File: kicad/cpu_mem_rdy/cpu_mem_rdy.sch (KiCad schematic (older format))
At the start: 37 parts, among them J1 USB, P1 CONN_02X04, P3 CONN_01X03, P4 CONN_02X02, P6 POWER, SW1 SW_PUSH, U1 65C02, U2 LM555N, U3 74HCT00, U4 74LS393, U6 28C256, U7 HM62256BLP-7, U8 HM62256BLP-7, X1 OSC

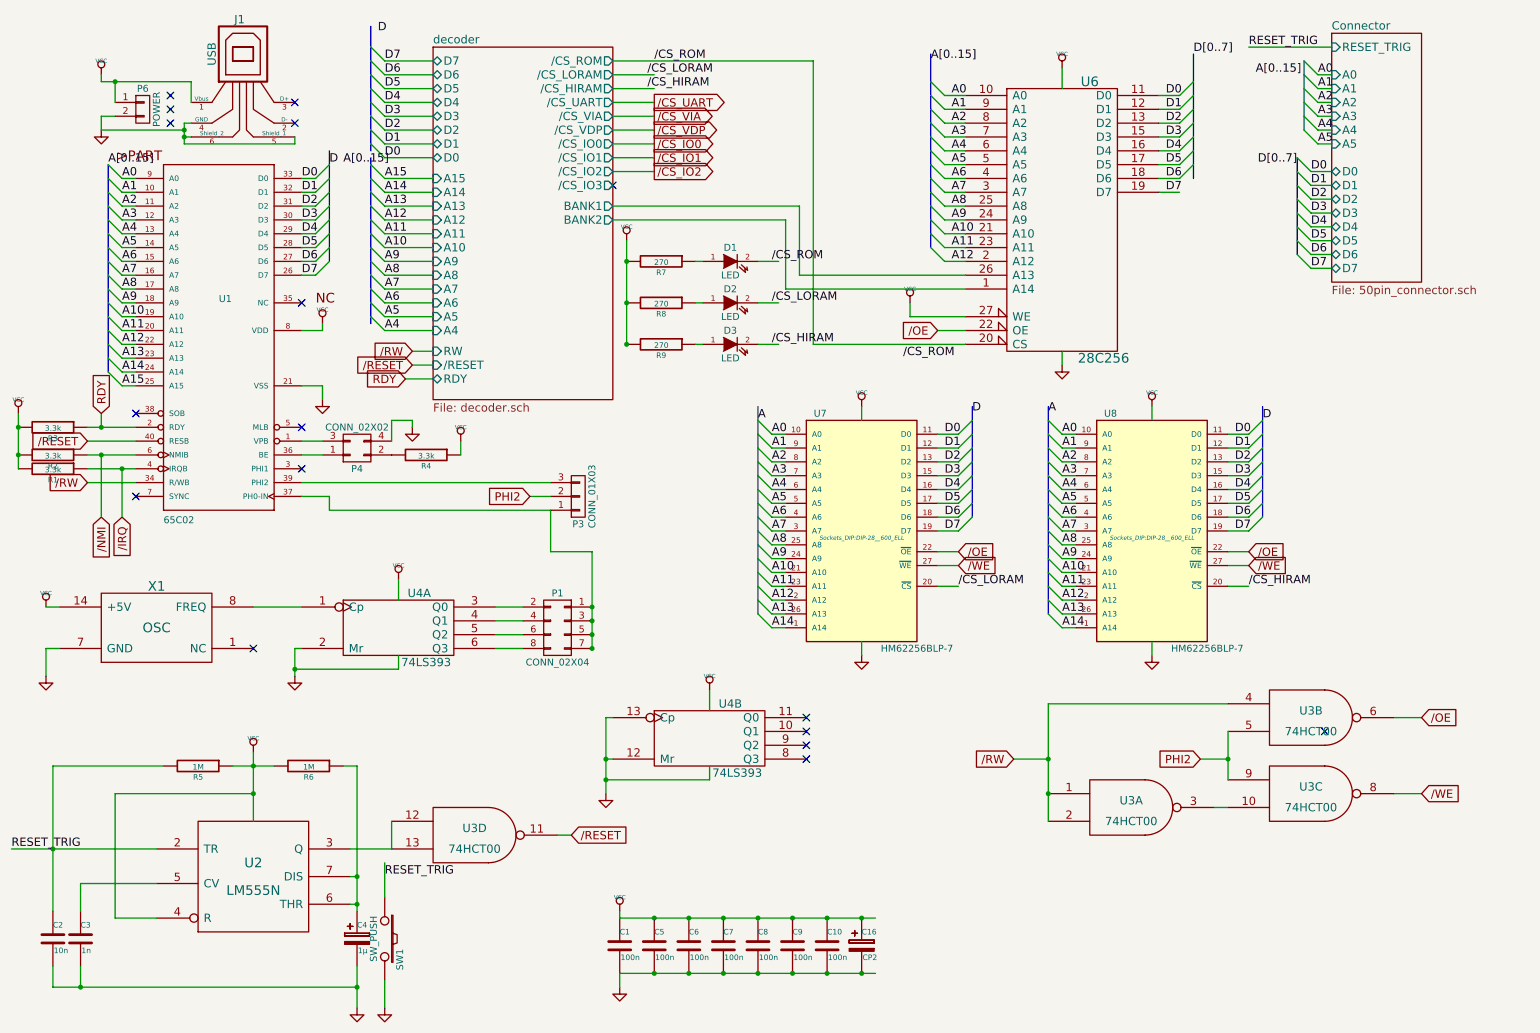
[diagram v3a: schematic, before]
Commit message: barrel jack
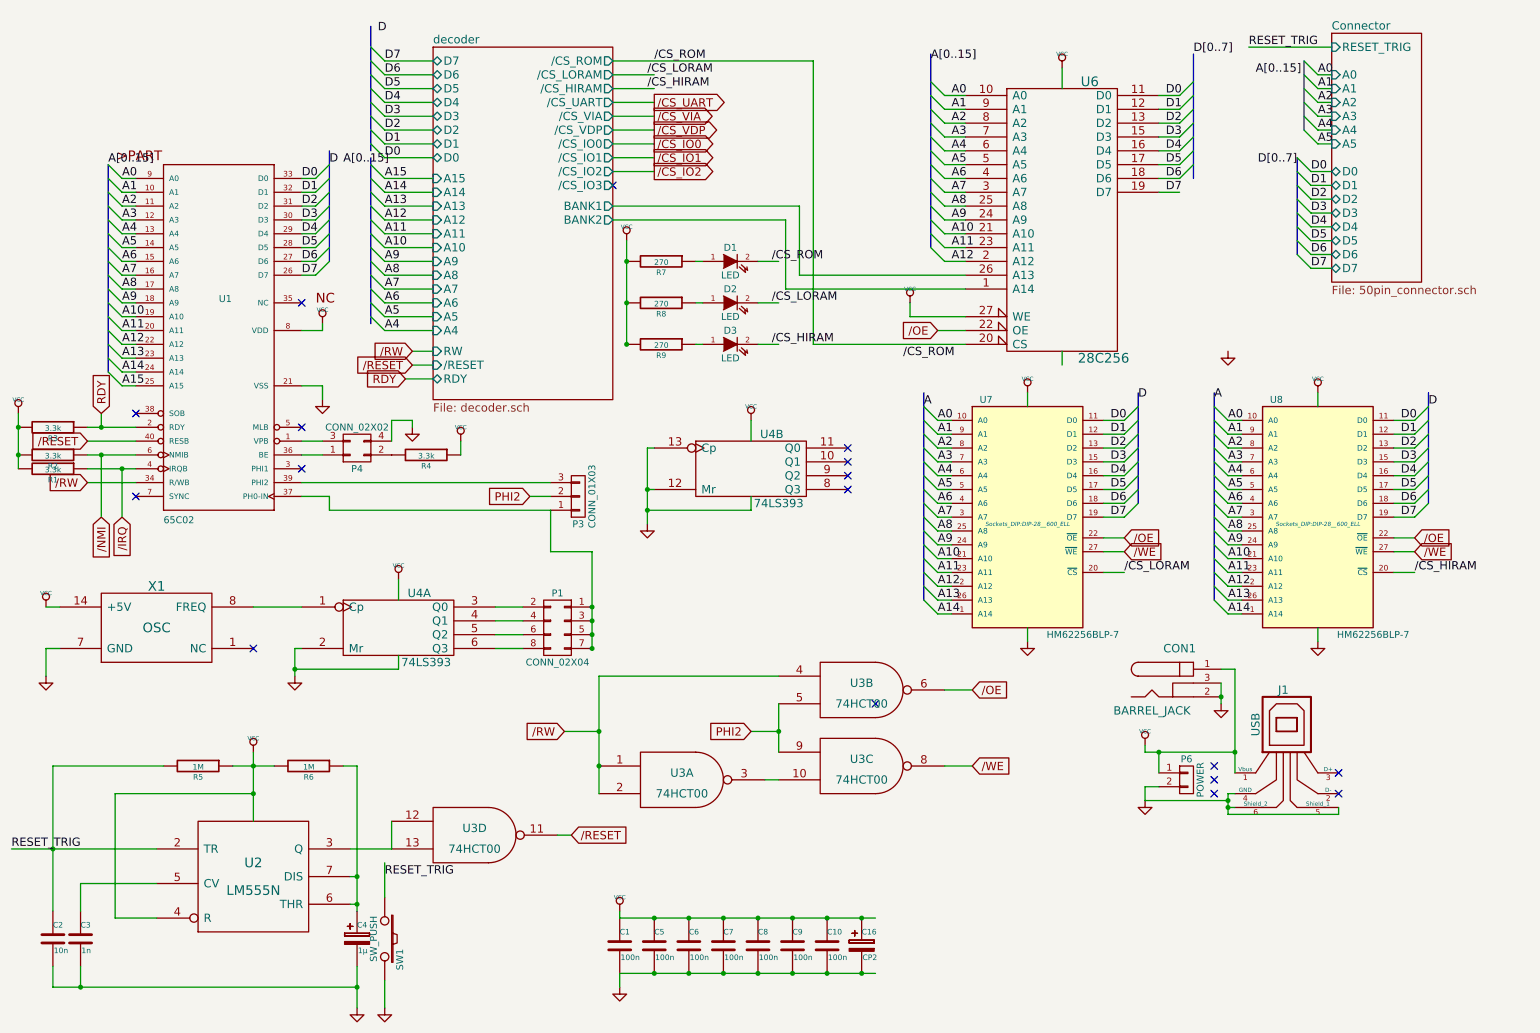
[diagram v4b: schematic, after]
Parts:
- added CON1: BARREL_JACK, Connect:BARREL_JACK, symbol BARREL_JACK
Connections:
- wire segments 261 -> 263
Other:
- moved on the sheet: J1, P6, U3A, U3B, U3C, U4B, U7, U8

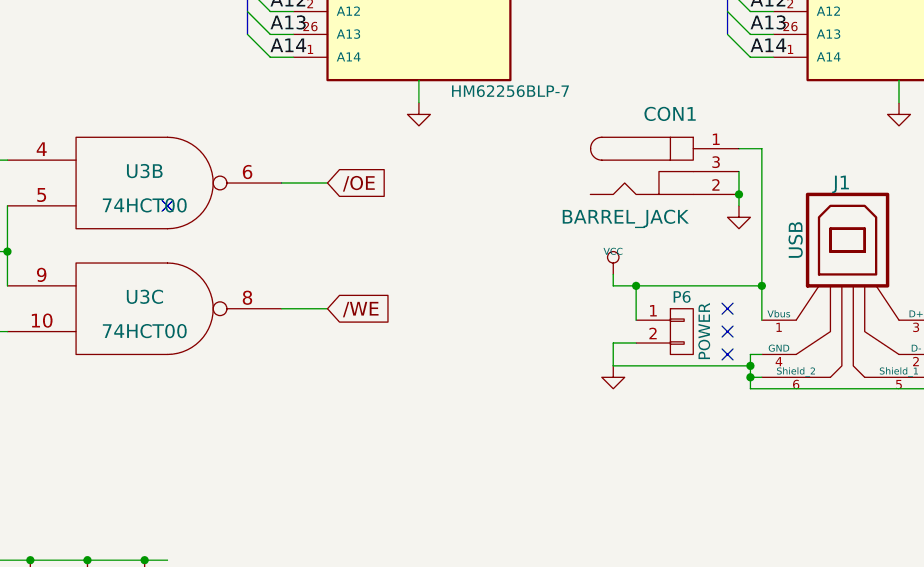
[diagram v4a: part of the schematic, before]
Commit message: connector for switch
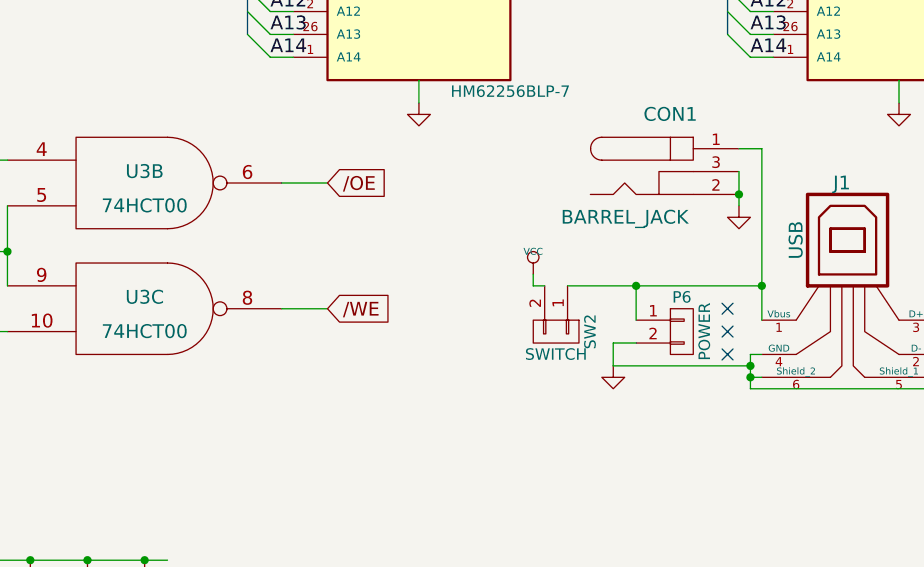
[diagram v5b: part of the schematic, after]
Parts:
- added SW2: SWITCH, Pin_Headers:Pin_Header_Straight_1x02, symbol CONN_01X02
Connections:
- wire segments 263 -> 264
- no-connect marks 17 -> 16
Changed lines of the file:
@@
 NoConn ~ 1400 3350
 NoConn ~ 1400 3950
-NoConn ~ 6750 5450
 $Comp
 L CONN_02X02 P4
@@
 L VCC #PWR026
 U 1 1 56B0EDB8
-P 8700 5750
-F 0 "#PWR026" H 8700 5850 30  0001 C CNN
-F 1 "VCC" H 8700 5850 30  0000 C CNN
-F 2 "" H 8700 5750 60  0000 C CNN
-F 3 "" H 8700 5750 60  0000 C CNN
-	1    8700 5750
+P 8350 5750
+F 0 "#PWR026" H 8350 5850 30  0001 C CNN
+F 1 "VCC" H 8350 5850 30  0000 C CNN
+F 2 "" H 8350 5750 60  0000 C CNN
+F 3 "" H 8350 5750 60  0000 C CNN
+	1    8350 5750
 	1    0    0    -1
 $EndComp
@@
 	8800 5950 8800 5800
 Wire Wire Line
-	8700 5800 9350 5800
+	8500 5800 9350 5800
 Connection ~ 8800 5800
-Wire Wire Line
-	8700 5800 8700 5750
 $Sheet
 S 10050 600  650  1800
@@
 $EndComp
 Connection ~ 9250 5400
+$Comp
+L CONN_01X02 SW2
+U 1 1 56BF480C
+P 8450 6000
+F 0 "SW2" H 8450 6150 50  0000 C CNN
+F 1 "SWITCH" V 8550 6000 50  0000 C CNN
+F 2 "Pin_Headers:Pin_Header_Straight_1x02" H 8450 6000 60  0001 C CNN
+F 3 "" H 8450 6000 60  0000 C CNN
+	1    8450 6000
+	0    1    1    0
+$EndComp
+Wire Wire Line
+	8400 5800 8350 5800
+Wire Wire Line
+	8350 5800 8350 5750
 $EndSCHEMATC

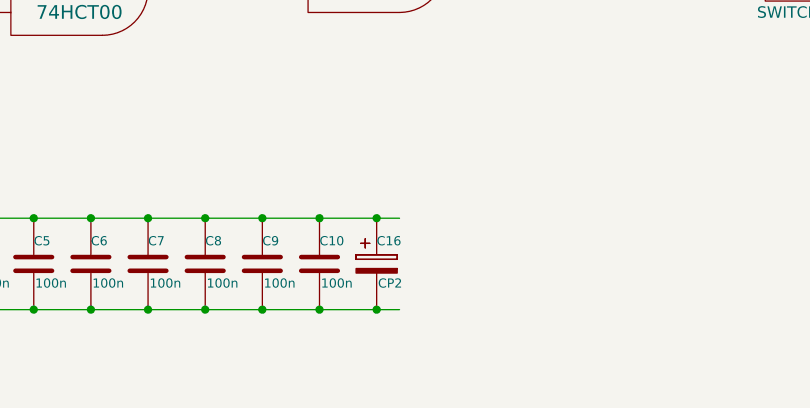
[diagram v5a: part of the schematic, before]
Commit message: C16 value
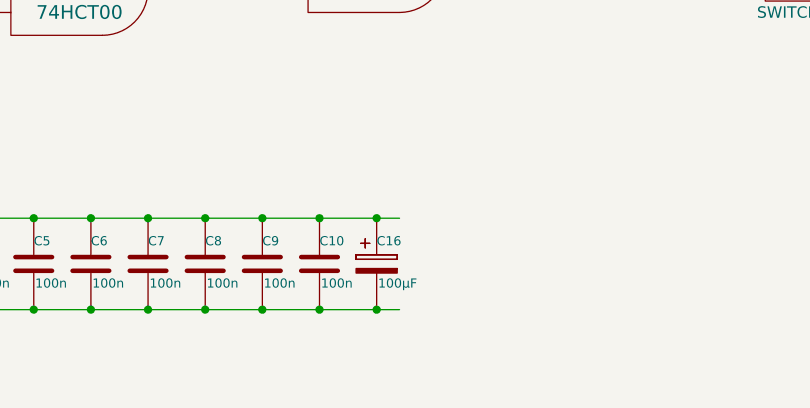
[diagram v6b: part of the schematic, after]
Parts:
- C16: value CP2 -> 100µF
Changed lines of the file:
@@
 LIBS:memory
 LIBS:xilinx
-LIBS:special
 LIBS:microcontrollers
 LIBS:dsp
@@
 P 6650 7200
 F 0 "C16" H 6650 7300 40  0000 L CNN
-F 1 "CP2" H 6656 7115 40  0000 L CNN
+F 1 "100µF" H 6656 7115 40  0000 L CNN
 F 2 "Capacitors_Elko_ThroughHole:Elko_vert_11.2x7.5mm_RM2.5" H 6688 7050 30  0001 C CNN
 F 3 "" H 6650 7200 60  0000 C CNN
